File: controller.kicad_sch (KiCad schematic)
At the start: 20 parts, among them J10 Conn_02x03_Counter_Clockwise, J7 SWD, J8 Conn_01x04_Male, J9 Conn_01x04_Male, SW1 Button, SW2 Button, U7 STM32G030Fx, Y1 8MHz

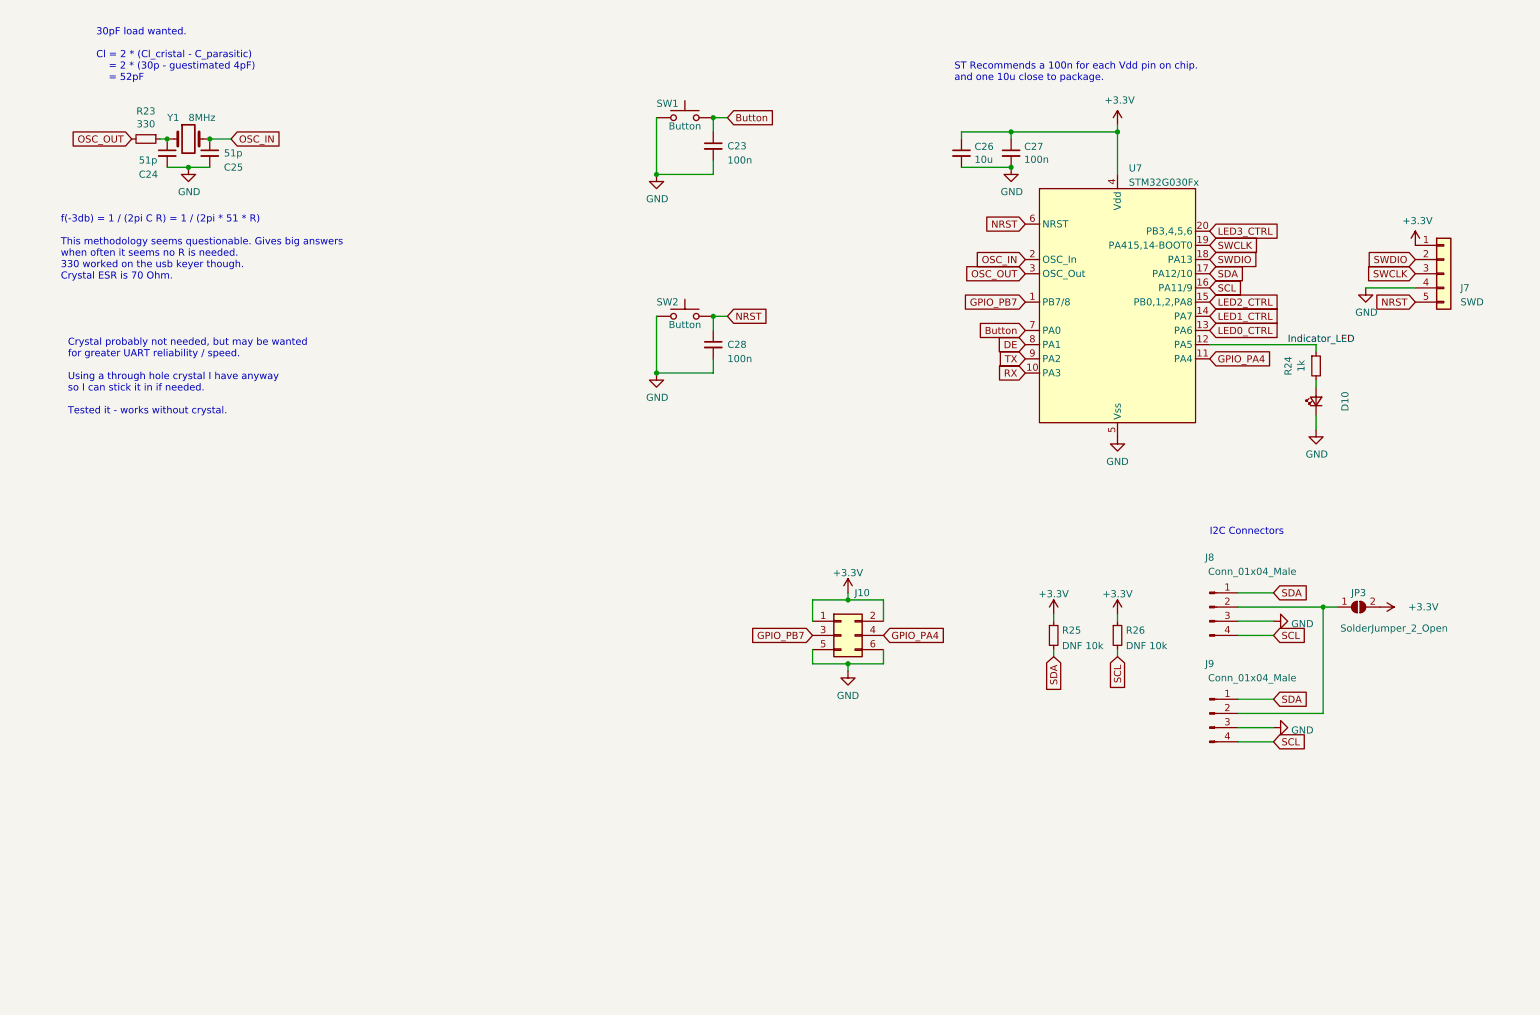
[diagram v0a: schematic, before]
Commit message: Schematic cleanup and readme improvement.
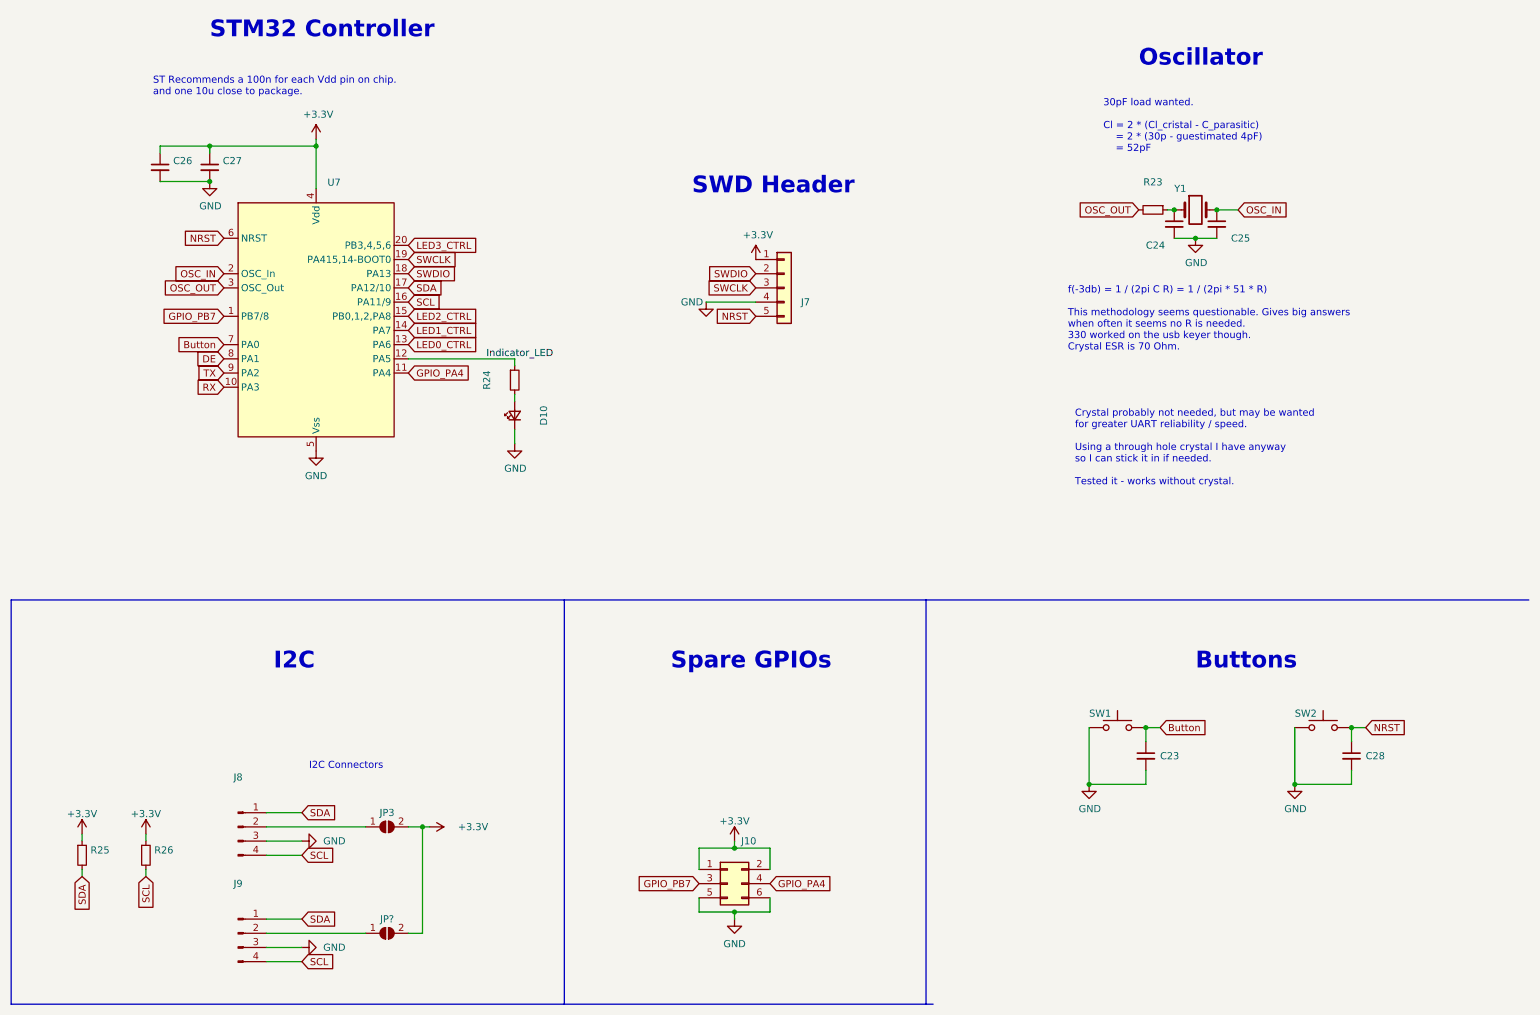
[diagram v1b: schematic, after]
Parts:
- added JP?: (no value), symbol Jumper:SolderJumper_2_Open
- C23, C27, C28: value 100n -> (none); footprint Capacitor_SMD:C_0805_2012Metric -> (none)
- C24, C25: value 51p -> (none); footprint Capacitor_SMD:C_0603_1608Metric_Pad1.08x0.95mm_HandSolder -> (none)
- C26: value 10u -> (none); footprint Capacitor_SMD:C_0805_2012Metric -> (none)
- D10: value ~ -> (none); footprint LED_SMD:LED_0805_2012Metric -> (none)
- J10: value Conn_02x03_Counter_Clockwise -> (none); footprint Connector_PinHeader_2.54mm:PinHeader_2x03_P2.54mm_Vertical -> (none)
- J7: value SWD -> (none); footprint Connector_PinHeader_2.54mm:PinHeader_1x05_P2.54mm_Vertical -> (none)
- J8, J9: value Conn_01x04_Male -> (none); footprint Connector_JST:JST_PH_B4B-PH-K_1x04_P2.00mm_Vertical -> (none)
- JP3: value SolderJumper_2_Open -> (none); footprint Jumper:SolderJumper-2_P1.3mm_Open_TrianglePad1.0x1.5mm -> (none)
- R23: value 330 -> (none); footprint Resistor_SMD:R_0805_2012Metric -> (none)
- R24: value 1k -> (none); footprint Resistor_SMD:R_0805_2012Metric -> (none)
- R25, R26: value DNF 10k -> (none); footprint Resistor_SMD:R_0805_2012Metric_Pad1.20x1.40mm_HandSolder -> (none)
- SW1, SW2: value Button -> (none); footprint Button_Switch_SMD:SW_SPST_TL3342 -> (none)
- U7: value STM32G030Fx -> (none); footprint Package_SO:TSSOP-20_4.4x6.5mm_P0.65mm -> (none)
- Y1: value 8MHz -> (none); footprint Crystal:Crystal_HC49-4H_Vertical -> (none)
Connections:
- net +3V3: now also JP?.2 (B)
- net at J8.2 (Pin_2), JP3.1 (A): no longer J9.2 (Pin_2)
- new net: J9.2 (Pin_2), JP?.1 (A)
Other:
- note added: "Buttons"
- note added: "I2C"
- note added: "Oscillator"
- note added: "STM32 Controller"
- note added: "SWD Header"
- note added: "Spare GPIOs"
- company: (none) -> River Cat
- title: (none) -> Plant Light LED Driver
- moved on the sheet: C23, C24, C25, C26, C27, C28, D10, J10, J7, J8, J9, JP3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
